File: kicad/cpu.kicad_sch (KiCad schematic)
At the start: 16 parts, among them U1 74AC04, U2 74AC245, U3 74AC573, U4 W65C816S, U5 DS1813-5+, X1 MXO45HS

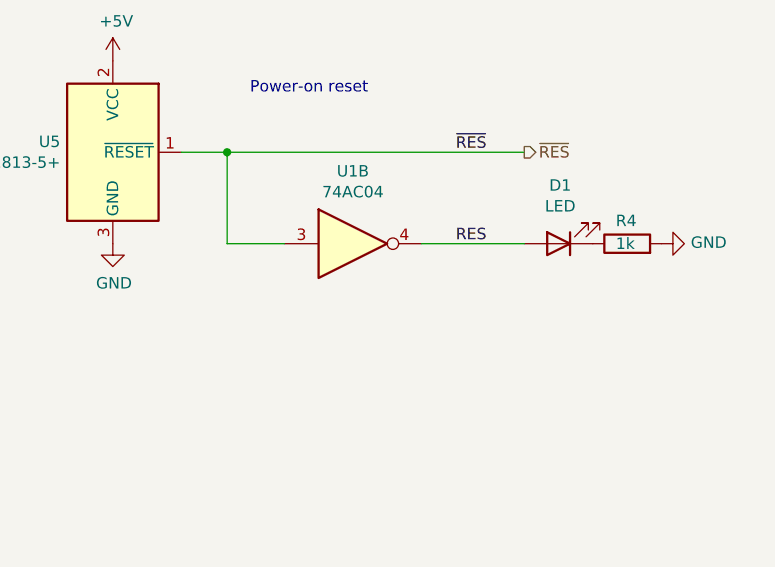
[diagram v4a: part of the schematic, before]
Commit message: connect UART to circuit
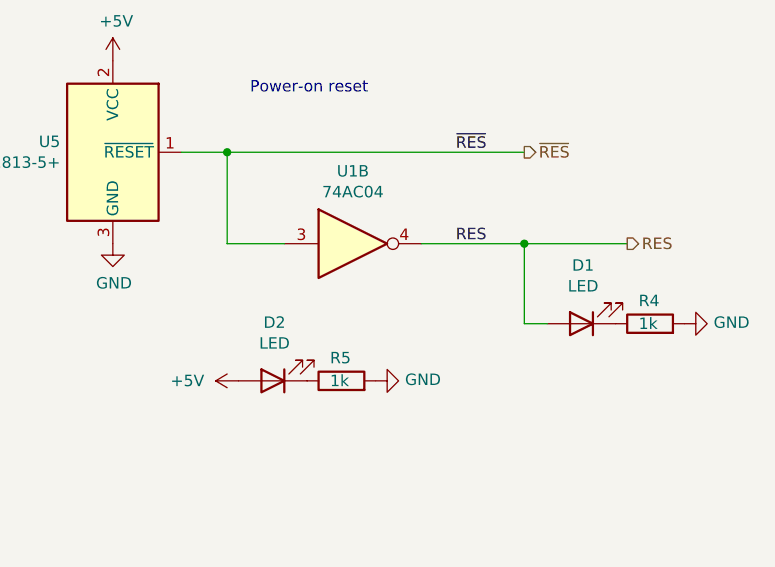
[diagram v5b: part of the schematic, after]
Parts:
- added D2: LED, symbol Device:LED
- added R5: 1k, symbol Device:R
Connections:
- net +5V: now also D2.2 (A)
- net GND: now also R5.2
- new net: D2.1 (K), R5.1
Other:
- moved on the sheet: D1, R4
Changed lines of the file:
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@@
 (kicad_sch (version 20211123) (generator eeschema)
   (paper "A4")
+  (junction (at 236.22 143.51) (diameter 0) (color 0 0 0 0)
+  )
   (junction (at 237.49 92.71) (diameter 0) (color 0 0 0 0)
   )
@@
     (stroke (width 0) (type default) (color 0 0 0 0))
   )
+  (wire (pts (xy 236.22 143.51) (xy 236.22 152.4))
+    (stroke (width 0) (type default) (color 0 0 0 0))
+  )
   (bus (pts (xy 99.06 39.37) (xy 99.06 48.26))
     (stroke (width 0) (type default) (color 0 0 0 0))
@@
     (stroke (width 0) (type default) (color 0 0 0 0))
   )
+  (wire (pts (xy 236.22 143.51) (xy 247.65 143.51))
+    (stroke (width 0) (type default) (color 0 0 0 0))
+  )
   (bus (pts (xy 80.01 46.99) (xy 80.01 49.53))
     (stroke (width 0) (type default) (color 0 0 0 0))
@@
   )
   (bus (pts (xy 186.69 67.31) (xy 199.39 67.31))
+    (stroke (width 0) (type default) (color 0 0 0 0))
+  )
+  (wire (pts (xy 236.22 152.4) (xy 238.76 152.4))
     (stroke (width 0) (type default) (color 0 0 0 0))
   )
@@
   (hierarchical_label "~{NMI}" (shape input) (at 48.26 69.85 180)
     (effects (font (size 1.27 1.27)) (justify right))
+  )
+  (hierarchical_label "RES" (shape output) (at 247.65 143.51 0)
+    (effects (font (size 1.27 1.27)) (justify left))
   )
   (hierarchical_label "~{RES}" (shape output) (at 236.22 133.35 0)
@@
   (symbol (lib_id "power:GND") (at 50.8 152.4 0) (unit 1)
     (in_bom yes) (on_board yes)
-    (property "Reference" "#PWR014" (id 0) (at 50.8 158.75 0)
+    (property "Reference" "#PWR013" (id 0) (at 50.8 158.75 0)
       (effects (font (size 1.27 1.27)) hide)
     )
@@
     (pin "1")
   )
-  (symbol (lib_id "Device:LED") (at 240.03 143.51 180) (unit 1)
-    (in_bom yes) (on_board yes)
-    (property "Reference" "D1" (id 0) (at 240.2078 137.033 0))
-    (property "Value" "LED" (id 1) (at 240.2078 139.3444 0))
-    (property "Footprint" "" (id 2) (at 240.03 143.51 0)
-      (effects (font (size 1.27 1.27)) hide)
-    )
-    (property "Datasheet" "~" (id 3) (at 240.03 143.51 0)
+  (symbol (lib_id "Device:LED") (at 242.57 152.4 180) (unit 1)
+    (in_bom yes) (on_board yes)
+    (property "Reference" "D1" (id 0) (at 242.7478 145.923 0))
+    (property "Value" "LED" (id 1) (at 242.7478 148.2344 0))
+    (property "Footprint" "" (id 2) (at 242.57 152.4 0)
+      (effects (font (size 1.27 1.27)) hide)
+    )
+    (property "Datasheet" "~" (id 3) (at 242.57 152.4 0)
       (effects (font (size 1.27 1.27)) hide)
     )
@@
     (pin "2")
   )
-  (symbol (lib_id "Device:R") (at 247.65 143.51 90) (unit 1)
-    (in_bom yes) (on_board yes)
-    (property "Reference" "R4" (id 0) (at 246.38 140.97 90)
+  (symbol (lib_id "Device:R") (at 250.19 152.4 90) (unit 1)
+    (in_bom yes) (on_board yes)
+    (property "Reference" "R4" (id 0) (at 248.92 149.86 90)
       (effects (font (size 1.27 1.27)) (justify right))
     )
-    (property "Value" "1k" (id 1) (at 246.38 143.51 90)
+    (property "Value" "1k" (id 1) (at 248.92 152.4 90)
       (effects (font (size 1.27 1.27)) (justify right))
     )
-    (property "Footprint" "" (id 2) (at 247.65 145.288 90)
-      (effects (font (size 1.27 1.27)) hide)
-    )
-    (property "Datasheet" "~" (id 3) (at 247.65 143.51 0)
+    (property "Footprint" "" (id 2) (at 250.19 154.178 90)
+      (effects (font (size 1.27 1.27)) hide)
+    )
+    (property "Datasheet" "~" (id 3) (at 250.19 152.4 0)
       (effects (font (size 1.27 1.27)) hide)
     )
@@
     (pin "2")
   )
-  (symbol (lib_id "power:GND") (at 251.46 143.51 90) (unit 1)
-    (in_bom yes) (on_board yes)
-    (property "Reference" "#PWR013" (id 0) (at 257.81 143.51 0)
-      (effects (font (size 1.27 1.27)) hide)
-    )
-    (property "Value" "GND" (id 1) (at 254.7112 143.383 90)
+  (symbol (lib_id "power:GND") (at 254 152.4 90) (unit 1)
+    (in_bom yes) (on_board yes)
+    (property "Reference" "#PWR014" (id 0) (at 260.35 152.4 0)
+      (effects (font (size 1.27 1.27)) hide)
+    )
+    (property "Value" "GND" (id 1) (at 257.2512 152.273 90)
       (effects (font (size 1.27 1.27)) (justify right))
     )
-    (property "Footprint" "" (id 2) (at 251.46 143.51 0)
-      (effects (font (size 1.27 1.27)) hide)
-    )
-    (property "Datasheet" "" (id 3) (at 251.46 143.51 0)
+    (property "Footprint" "" (id 2) (at 254 152.4 0)
+      (effects (font (size 1.27 1.27)) hide)
+    )
+    (property "Datasheet" "" (id 3) (at 254 152.4 0)
       (effects (font (size 1.27 1.27)) hide)
     )
@@
   (symbol (lib_id "power:+5V") (at 72.39 165.1 0) (unit 1)
     (in_bom yes) (on_board yes)
-    (property "Reference" "#PWR016" (id 0) (at 72.39 168.91 0)
+    (property "Reference" "#PWR018" (id 0) (at 72.39 168.91 0)
       (effects (font (size 1.27 1.27)) hide)
     )
@@
   (symbol (lib_id "power:GND") (at 135.89 176.53 0) (unit 1)
     (in_bom yes) (on_board yes)
-    (property "Reference" "#PWR017" (id 0) (at 135.89 182.88 0)
+    (property "Reference" "#PWR019" (id 0) (at 135.89 182.88 0)
       (effects (font (size 1.27 1.27)) hide)
     )
@@
   (symbol (lib_id "power:GND") (at 151.13 186.69 0) (unit 1)
     (in_bom yes) (on_board yes)
-    (property "Reference" "#PWR018" (id 0) (at 151.13 193.04 0)
+    (property "Reference" "#PWR020" (id 0) (at 151.13 193.04 0)
       (effects (font (size 1.27 1.27)) hide)
     )
@@
   (symbol (lib_id "power:+5V") (at 151.13 161.29 0) (unit 1)
     (in_bom yes) (on_board yes)
-    (property "Reference" "#PWR015" (id 0) (at 151.13 165.1 0)
+    (property "Reference" "#PWR017" (id 0) (at 151.13 165.1 0)
       (effects (font (size 1.27 1.27)) hide)
     )
@@
       (effects (font (size 1.27 1.27)) hide)
     )
+    (pin "1")
+  )
+  (symbol (lib_id "power:GND") (at 219.71 158.75 90) (unit 1)
+    (in_bom yes) (on_board yes)
+    (property "Reference" "#PWR016" (id 0) (at 226.06 158.75 0)
+      (effects (font (size 1.27 1.27)) hide)
+    )
+    (property "Value" "GND" (id 1) (at 222.9612 158.623 90)
+      (effects (font (size 1.27 1.27)) (justify right))
+    )
+    (property "Footprint" "" (id 2) (at 219.71 158.75 0)
+      (effects (font (size 1.27 1.27)) hide)
+    )
+    (property "Datasheet" "" (id 3) (at 219.71 158.75 0)
+      (effects (font (size 1.27 1.27)) hide)
+    )
+    (pin "1")
+  )
+  (symbol (lib_id "Device:LED") (at 208.28 158.75 180) (unit 1)
+    (in_bom yes) (on_board yes)
+    (property "Reference" "D2" (id 0) (at 208.4578 152.273 0))
+    (property "Value" "LED" (id 1) (at 208.4578 154.5844 0))
+    (property "Footprint" "" (id 2) (at 208.28 158.75 0)
+      (effects (font (size 1.27 1.27)) hide)
+    )
+    (property "Datasheet" "~" (id 3) (at 208.28 158.75 0)
+      (effects (font (size 1.27 1.27)) hide)
+    )
+    (pin "1")
+    (pin "2")
+  )
+  (symbol (lib_id "Device:R") (at 215.9 158.75 90) (unit 1)
+    (in_bom yes) (on_board yes)
+    (property "Reference" "R5" (id 0) (at 214.63 156.21 90)
+      (effects (font (size 1.27 1.27)) (justify right))
+    )
+    (property "Value" "1k" (id 1) (at 214.63 158.75 90)
+      (effects (font (size 1.27 1.27)) (justify right))
+    )
+    (property "Footprint" "" (id 2) (at 215.9 160.528 90)
+      (effects (font (size 1.27 1.27)) hide)
+    )
+    (property "Datasheet" "~" (id 3) (at 215.9 158.75 0)
+      (effects (font (size 1.27 1.27)) hide)
+    )
+    (pin "1")
+    (pin "2")
+  )
+  (symbol (lib_id "power:+5V") (at 204.47 158.75 90) (unit 1)
+    (in_bom yes) (on_board yes) (fields_autoplaced)
+    (property "Reference" "#PWR015" (id 0) (at 208.28 158.75 0)
+      (effects (font (size 1.27 1.27)) hide)
+    )
+    (property "Value" "+5V" (id 1) (at 200.66 158.7499 90)
+      (effects (font (size 1.27 1.27)) (justify left))
+    )
+    (property "Footprint" "" (id 2) (at 204.47 158.75 0)
+      (effects (font (size 1.27 1.27)) hide)
+    )
+    (property "Datasheet" "" (id 3) (at 204.47 158.75 0)
+      (effects (font (size 1.27 1.27)) hide)
+    )
